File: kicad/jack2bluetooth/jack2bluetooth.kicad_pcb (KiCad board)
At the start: 4 copper layers, 83 x 53 mm, 108 parts, among them IC1 TLV320AIC3101IRHBR, IC2 BQ25619RTWR, IC3 ESP32-C6-WROOM-1-N8, IC4 TPS62A01PDDCR, IC5 TPS62A01PDDCR, IC6 DS04-254-2-02BK-SMT, J1 SJ1-2503A, J2 USB_C_Receptacle, J3 Conn_01x04_Pin, J4 SJ3-35063A, J5 Conn_01x03_Pin, J6 Conn_01x04_Pin, J7 Conn_01x02_Pin, J9 Conn_01x08_Pin, Q1 DMP3099L-13, SW1 SW_Push, SW2 SW_Push, SW3 SW_Push, SW5 SW_SPDT, SW6 SW_Push, U1 TLV75801PDBVR

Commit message: feat: remove warnings in ERC errors and warnings in schematic. refresh layout
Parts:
- removed D6: PRTR5V0U2X, Package_TO_SOT_SMD:SOT-143
- removed IC6: DS04-254-2-02BK-SMT, DIP-switch-2:DS04254202BKSMT
- removed JP2: jumper_RCOM, Connector_PinHeader_2.54mm:PinHeader_1x02_P2.54mm_Vertical
- removed JP3: jumper_ROUT, Connector_PinHeader_2.54mm:PinHeader_1x02_P2.54mm_Vertical
- removed JP4: jumper_LCOM, Connector_PinHeader_2.54mm:PinHeader_1x02_P2.54mm_Vertical
- removed JP5: jumper_LOUT, Connector_PinHeader_2.54mm:PinHeader_1x02_P2.54mm_Vertical
- removed R30, R31: 0, Resistor_SMD:R_0805_2012Metric_Pad1.20x1.40mm_HandSolder
- removed U1: TLV75801PDBVR, TLV75801PDBVR:SOT95P280X145-5N
- added C34: 1u, Capacitor_SMD:C_0805_2012Metric_Pad1.18x1.45mm_HandSolder, F.Cu at (-78.2, 10.3)
- added C35: 0.1uF, Capacitor_SMD:C_0805_2012Metric_Pad1.18x1.45mm_HandSolder, F.Cu at (-78.2, 13.3)
- added C38: 0.1uF, Capacitor_SMD:C_0805_2012Metric_Pad1.18x1.45mm_HandSolder, F.Cu at (-78.2, 16.3)
- added C39: 1uF, Capacitor_SMD:C_0805_2012Metric_Pad1.18x1.45mm_HandSolder, F.Cu at (-78.2, 19.3)
- added C40: 1uF, Capacitor_SMD:C_0805_2012Metric_Pad1.18x1.45mm_HandSolder, F.Cu at (-78.2, 22.4)
- added C41: 1uF, Capacitor_SMD:C_0805_2012Metric_Pad1.18x1.45mm_HandSolder, F.Cu at (-78.2, 25.4)
- added C42: 1uF, Capacitor_SMD:C_0805_2012Metric_Pad1.18x1.45mm_HandSolder, F.Cu at (-78.2, 28.4)
- added C43: 100uF, Capacitor_SMD:C_0805_2012Metric_Pad1.18x1.45mm_HandSolder, F.Cu at (129.9, 298.7)
- added D2: LED - green, LED_SMD:LED_0805_2012Metric_Pad1.15x1.40mm_HandSolder, F.Cu at (-53.2, 41.3)
- added D3: 1N5819, Diode_SMD:D_SOD-123, F.Cu at (171.0, 97.5)
- added F1: Polyfuse, Fuse:Fuse_1210_3225Metric_Pad1.42x2.65mm_HandSolder, F.Cu at (165.0, 97.5)
- added F2: Polyfuse, Fuse:Fuse_1210_3225Metric_Pad1.42x2.65mm_HandSolder, F.Cu at (141.4, 302.2)
- added IC7: ESP32-WROVER-E-N16R8, ESP32-WROVER-E-N16R8:ESP32WROVEREN16R8, F.Cu at (29.9, 51.2)
- added J10: Conn_01x03_Pin, Connector_PinHeader_2.54mm:PinHeader_1x03_P2.54mm_Vertical, F.Cu at (-59.5, 56.5)
- added J8: Conn_01x02_Pin, Connector_PinHeader_2.00mm:PinHeader_1x02_P2.00mm_Vertical, F.Cu at (-66.0, 82.0)
- added PS1: TLV75801PDBVR, TLV75801PDBVR:SOT95P280X145-5N, F.Cu at (341.2, 34.0)
- added Q2: BC846, Package_TO_SOT_SMD:SOT-23, F.Cu at (-128.2, 8.50)
- added Q3: BC846, Package_TO_SOT_SMD:SOT-23, F.Cu at (-136.2, 10.5)
- added SW4: SW_Push, Button_Switch_THT:SW_PUSH_6mm, F.Cu at (-100.7, 45.3)
- added SW7: SW_SPDT, SLW-10558:SLW-105558-2A-N-D, F.Cu at (30.0, 114.5)
- added TP1: TestPoint, TestPoint:TestPoint_Pad_D1.0mm, F.Cu at (123.5, -41.1)
- added TP10: TestPoint, TestPoint:TestPoint_Pad_D1.0mm, F.Cu at (191.4, 297.3)
- added TP11: TestPoint, TestPoint:TestPoint_Pad_D1.0mm, F.Cu at (191.4, 300.3)
- added TP12: TestPoint, TestPoint:TestPoint_Pad_D1.0mm, F.Cu at (191.4, 303.4)
- added TP13: TestPoint, TestPoint:TestPoint_Pad_D1.0mm, F.Cu at (191.4, 306.4)
- added TP14: TestPoint, TestPoint:TestPoint_Pad_D1.0mm, F.Cu at (191.4, 309.5)
- added TP15: TestPoint, TestPoint:TestPoint_Pad_D1.0mm, F.Cu at (194.5, 291.2)
- added TP16: TestPoint, TestPoint:TestPoint_Pad_D1.0mm, F.Cu at (194.5, 294.2)
- added TP17: TestPoint, TestPoint:TestPoint_Pad_D1.0mm, F.Cu at (194.5, 297.3)
- added TP18: TestPoint, TestPoint:TestPoint_Pad_D1.0mm, F.Cu at (194.5, 300.3)
- added TP19: TestPoint, TestPoint:TestPoint_Pad_D1.0mm, F.Cu at (194.5, 303.4)
- added TP2: TestPoint, TestPoint:TestPoint_Pad_D1.0mm, F.Cu at (123.5, -38.1)
- added TP20: TestPoint, TestPoint:TestPoint_Pad_D1.0mm, F.Cu at (194.5, 306.4)
- added TP21: TestPoint, TestPoint:TestPoint_Pad_D1.0mm, F.Cu at (194.5, 309.5)
- added TP22: TestPoint, TestPoint:TestPoint_Pad_D1.0mm, F.Cu at (185.9, 312.2)
- added TP23: TestPoint, TestPoint:TestPoint_Pad_D1.0mm, F.Cu at (213.9, 33.9)
- added TP24: TestPoint, TestPoint:TestPoint_Pad_D1.0mm, F.Cu at (213.9, 37.0)
- added TP25: TestPoint, TestPoint:TestPoint_Pad_D1.0mm, F.Cu at (213.9, 40.0)
- added TP26: TestPoint, TestPoint:TestPoint_Pad_D1.0mm, F.Cu at (213.9, 43.0)
- added TP27: TestPoint, TestPoint:TestPoint_Pad_D1.0mm, F.Cu at (213.9, 46.1)
- added TP28: TestPoint, TestPoint:TestPoint_Pad_D1.0mm, F.Cu at (213.9, 49.1)
- added TP29: TestPoint, TestPoint:TestPoint_Pad_D1.0mm, F.Cu at (217.0, 30.9)
- added TP3: TestPoint, TestPoint:TestPoint_Pad_D1.0mm, F.Cu at (123.5, -35.0)
- added TP30: TestPoint, TestPoint:TestPoint_Pad_D1.0mm, F.Cu at (217.0, 33.9)
- added TP31: TestPoint, TestPoint:TestPoint_Pad_D1.0mm, F.Cu at (217.0, 37.0)
- added TP32: TestPoint, TestPoint:TestPoint_Pad_D1.0mm, F.Cu at (217.0, 40.0)
- added TP33: TestPoint, TestPoint:TestPoint_Pad_D1.0mm, F.Cu at (217.0, 43.0)
- added TP34: TestPoint, TestPoint:TestPoint_Pad_D1.0mm, F.Cu at (217.0, 46.1)
- added TP4: TestPoint, TestPoint:TestPoint_Pad_D1.0mm, F.Cu at (123.5, -32.0)
- added TP5: TestPoint, TestPoint:TestPoint_Pad_D1.0mm, F.Cu at (123.5, -28.9)
- added TP6: TestPoint, TestPoint:TestPoint_Pad_D1.0mm, F.Cu at (123.5, -25.9)
- added TP7: TestPoint, TestPoint:TestPoint_Pad_D1.0mm, F.Cu at (123.5, -22.9)
- added TP8: TestPoint, TestPoint:TestPoint_Pad_D1.0mm, F.Cu at (191.4, 291.2)
- added TP9: TestPoint, TestPoint:TestPoint_Pad_D1.0mm, F.Cu at (191.4, 294.2)
- D1, D4, D7, D8, J7, J9, R7, R8: moved to F.Cu
- D5: value PRTR5V0U2X -> SMF5V0A-E3-08; footprint Package_TO_SOT_SMD:SOT-143 -> LIB_SMF5V0A-E3-08:SMF5V0AE308
- IC1: footprint TLV320AIC3101:QFN50P500X500X100-33N-D -> TLV320AIC3101IRHBR:QFN50P500X500X100-33N-D
- IC3: value ESP32-C6-WROOM-1-N8 -> MCP23008T-E_SO; footprint ESP32-C6-WROOM-1:ESP32C6WROOM1N8 -> LIB_MCP23008T-E_SO:SOIC127P1030X265-18N
- IC4, IC5: footprint TPS62A01PDDRC:SOT95P280X110-6N -> TPS62A01PDDCR:SOT95P280X110-6N
- J1: value SJ1-2503A -> SJ3-35063A; footprint SJ1-2503A:SJ12503A -> LIB_SJ3-35063A:SJ335063A
- J3: value Conn_01x04_Pin -> Conn_01x03_Pin; footprint Connector_PinHeader_2.54mm:PinHeader_1x04_P2.54mm_Vertical -> Connector_PinHeader_2.54mm:PinHeader_1x03_P2.54mm_Vertical
- J4: value SJ3-35063A -> SJ1-2503A; footprint SJ3-35063A:SJ335063A -> LIB_SJ1-2503A:SJ12503A
- Q1: footprint DMP3099L:SOT96P240X115-3N -> DMP3099L-13:SOT96P240X115-3N
- R10: value 0 -> 10k
- R12, R18: value 10k -> 0
- R9: value 0 -> 1k
- moved SW6 316.5 mm to (-117.5, 46.8)
- moved R12 309.9 mm to (-58.2, 16.2)
- moved R10 306.6 mm to (-58.2, 13.2), turned to 0 degrees
- moved R9 305.9 mm to (-58.2, 10.3), turned to 0 degrees
- moved R17 296.9 mm to (-58.2, 22.1), turned to 0 degrees
- moved R16 296.6 mm to (-58.2, 19.1), turned to 0 degrees
- moved J3 283.1 mm to (-89.9, 45.6), turned to 0 degrees
- moved R18 244.2 mm to (-58.2, 25.0), turned to 0 degrees
- moved Q1 237.4 mm to (-58.1, 42.1)
- moved D4 174.0 mm to (123.0, 252.7), turned to 0 degrees
- moved R7 168.0 mm to (115.2, 254.0)
- moved R8 167.4 mm to (109.2, 254.0)
- moved C28 163.3 mm to (340.0, 41.5)
- moved C31 163.3 mm to (346.2, 38.7)
- moved C32 163.3 mm to (333.2, 45.2)
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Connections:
- net /BTST renamed TP_BTST
- net /SW renamed TP_SW
- net Net-(IC2-PMID) renamed TP_PMID
- net Net-(IC2-PMID_GOOD) renamed PMID_GOOD
- C1 pad 2: IO4 -> IO_EXP_1
- C10 pad 2: BAT- -> lcd_cs
- C11 pad 2: BAT- -> lcd_cs
- C16 pad 1: BAT- -> lcd_cs
- C17 pad 2: BAT- -> lcd_cs
- C2 pad 2: IO0 -> IO_EXP_0
- C20 pad 1: Net-(JP2-B) -> HPROUT
- C20 pad 2: jack35_right -> Net-(C20-Pad2)
- C21 pad 1: Net-(JP4-B) -> HPLOUT
- C21 pad 2: jack35_left -> Net-(C21-Pad2)
- C22 pad 1: BAT- -> lcd_cs
- C24 pad 2: BAT- -> lcd_cs
- C25 pad 1: IO1 -> IO_EXP_3
- C25 pad 2: BAT- -> lcd_cs
- C26 pad 1: BAT- -> lcd_cs
- C27 pad 2: BAT- -> lcd_cs
- C28 pad 2: BAT- -> lcd_cs
- C29 pad 2: BAT- -> lcd_cs
- C3 pad 2: IO5 -> IO_EXP_2
- C30 pad 2: BAT- -> lcd_cs
- C32 pad 2: BAT- -> lcd_cs
- C33 pad 2: BAT- -> lcd_cs
- C36 pad 2: BAT- -> lcd_cs
- C37 pad 2: BAT- -> lcd_cs
- C4 pad 2: BAT- -> lcd_cs
- C5 pad 2: BAT- -> lcd_cs
- C6 pad 2: BAT- -> lcd_cs
- C7 pad 2: BAT- -> lcd_cs
- C8 pad 2: LINE2R -> Net-(C8-Pad2)
- C9 pad 2: LINE2L -> Net-(C9-Pad2)
- D1 pad 1: BAT- -> lcd_cs
- D4 pad 2: led_adc -> IO_EXP_4
- D5 pad 1: BAT- -> lcd_cs
- D5 pad 2: USB_DN -> /usb_vbus
- D7 pad 2: led_dac -> IO_EXP_5
- IC1 pad 1: IO19 -> TXD0
- IC1 pad 2: IO20 -> IO2
- IC1 pad 20: HPLCOM -> unconnected-(IC1-HPLCOM-Pad20)
- IC1 pad 22: HPRCOM -> unconnected-(IC1-HPRCOM-Pad22)
- IC1 pad 3: IO21 -> IO4
- IC1 pad 31: IO18 -> IO_EXP_7
- IC1 pad 4: IO22 -> IO5
- IC1 pad 5: IO23 -> IO18
- IC1 pad 6: BAT- -> lcd_cs
- IC1 pad 8: IO7 -> IO21
- IC1 pad 9: IO6 -> IO19
- IC2 pad 15: SYSTEM -> PMIC_SYSTEM
- IC2 pad 16: SYSTEM -> PMIC_SYSTEM
- IC2 pad 17: BAT- -> lcd_cs
- IC2 pad 18: BAT- -> lcd_cs
- IC2 pad 25: BAT- -> lcd_cs
- IC2 pad 5: IO7 -> IO21
- IC2 pad 6: IO6 -> IO19
- IC2 pad 7: IO10 -> IO39
- IC2 pad 9: IO11 -> IO27
- IC3 pad 1: BAT- -> IO21
- IC3 pad 10: IO8 -> IO_EXP_0
- IC3 pad 11: IO10 -> IO_EXP_1
- IC3 pad 12: IO11 -> IO_EXP_2
- IC3 pad 13: USB_DN -> IO_EXP_3
- IC3 pad 14: USB_DP -> IO_EXP_4
- IC3 pad 15: IO9 -> IO_EXP_5
- IC3 pad 16: IO18 -> IO_EXP_6
- IC3 pad 17: IO19 -> IO_EXP_7
- IC3 pad 18: IO20 -> Net-(IC3-VDD)
- IC3 pad 2: +3.3V -> IO19
- IC3 pad 3: mcu_enable -> lcd_cs
- IC3 pad 4: IO4 -> lcd_cs
- IC3 pad 5: IO5 -> lcd_cs
- IC3 pad 6: IO6 -> IO32
- IC3 pad 7: IO7 -> unconnected-(IC3-NC-Pad7)
- IC3 pad 8: IO0 -> IO36
- IC3 pad 9: IO1 -> lcd_cs
- IC4 pad 2: BAT- -> lcd_cs
- IC5 pad 2: BAT- -> lcd_cs
- J1 pad 2: jack25_left -> jack35_right
- J1 pad 3: jack25_left -> jack35_left
- J2 pad A1: BAT- -> lcd_cs
- J2 pad A12: BAT- -> lcd_cs
- J2 pad A4: VCC -> /usb_vbus
- J2 pad A6: USB_DP -> unconnected-(J2-D+-PadA6)
- J2 pad A7: USB_DN -> unconnected-(J2-D--PadA7)
- J2 pad A9: VCC -> /usb_vbus
- J2 pad B1: BAT- -> lcd_cs
- J2 pad B12: BAT- -> lcd_cs
- J2 pad B4: VCC -> /usb_vbus
- J2 pad B6: USB_DP -> unconnected-(J2-D+-PadB6)
- J2 pad B7: USB_DN -> unconnected-(J2-D--PadB7)
- J2 pad B9: VCC -> /usb_vbus
- J2 pad S1: BAT- -> lcd_cs
- J3 pad 1: VCC -> TXD0
- J3 pad 2: IO16 -> RXD0
- J3 pad 3: IO17 -> lcd_cs
- J4 pad 2: jack35_right -> jack25_left
- J4 pad 3: jack35_left -> jack25_left
- J5 pad 2: BAT- -> lcd_cs
- J5 pad 3: BAT+ -> Net-(J5-Pin_3)
- J6 pad 1: IO4 -> IO14
- J6 pad 2: IO5 -> IO12
- J6 pad 3: IO6 -> IO13
- J6 pad 4: IO7 -> IO15
- J7 pad 1: BAT- -> lcd_cs
- J9 pad 2: BAT- -> lcd_cs
- J9 pad 3: IO17 -> IO26
- J9 pad 4: IO15 -> IO25
- J9 pad 5: IO16 -> IO23
- J9 pad 6: IO3 -> IO22
- J9 pad 7: BAT- -> lcd_cs
- JP1 pad 3: BAT- -> lcd_cs
- Q1 pad 1: IO2 -> IO_EXP_6
- R1 pad 1: BAT- -> lcd_cs
- R1 pad 2: IO4 -> IO_EXP_1
- R10 pad 1: LINE2L -> REGN
- R10 pad 2: jack25_left -> Net-(JP1-A)
- R12 pad 1: REGN -> LINE2R
- R12 pad 2: Net-(JP1-A) -> Net-(C8-Pad2)
- R14 pad 2: BAT- -> lcd_cs
- R16 pad 1: jack35_right -> LINE2L
- R16 pad 2: Net-(JP2-B) -> Net-(C9-Pad2)
- R17 pad 1: jack35_left -> jack35_right
- R17 pad 2: Net-(JP4-B) -> Net-(C20-Pad2)
- R18 pad 1: IO9 -> jack35_left
- R18 pad 2: +3.3V -> Net-(C21-Pad2)
- R19 pad 1: IO7 -> IO21
- R2 pad 1: BAT- -> lcd_cs
- R2 pad 2: IO0 -> IO_EXP_0
- R20 pad 1: IO6 -> IO19
- R21 pad 1: IO8 -> lcd_cs
- R21 pad 2: +3.3V -> Net-(Q2-B)
- R23 pad 2: BAT- -> lcd_cs
- R29 pad 1: IO11 -> IO27
- R3 pad 1: BAT- -> lcd_cs
- R3 pad 2: IO5 -> IO_EXP_2
- R32 pad 1: IO10 -> IO39
- R34 pad 1: IO2 -> IO_EXP_6
- R37 pad 2: BAT- -> lcd_cs
- R40 pad 2: BAT- -> lcd_cs
- R5 pad 2: BAT- -> lcd_cs
- R6 pad 1: BAT- -> lcd_cs
- R7 pad 2: BAT- -> lcd_cs
- R8 pad 2: BAT- -> lcd_cs
- R9 pad 1: LINE2R -> SYSTEM
- R9 pad 2: jack25_right -> Net-(D2-A)
- SW1 pad 1: IO4 -> IO_EXP_1
- SW2 pad 1: IO0 -> IO_EXP_0
- SW3 pad 1: IO5 -> IO_EXP_2
- SW5 pad 2: IO1 -> IO_EXP_3
- SW5 pad 3: BAT- -> lcd_cs
- SW6 pad 1: BAT- -> lcd_cs
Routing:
- net BAT-: track 167.8 -> 0.00 mm, vias 38 -> 0
- net nQON: track 108.2 -> 0.00 mm, vias 1 -> 0
- net IO7: track 104.7 -> 0.00 mm, vias 3 -> 0
- net IO9: track 102.0 -> 0.00 mm, vias 5 -> 0
- net IO6: track 101.2 -> 0.00 mm, vias 3 -> 0
- net IO8: track 93.5 -> 0.00 mm, vias 3 -> 0
- net IO5: track 90.7 -> 0.00 mm, vias 2 -> 0
- net Net-(D1-A): track 86.9 -> 0.00 mm, vias 1 -> 0
- net STAT: track 78.7 -> 0.00 mm, vias 1 -> 0
- net IO17: track 72.9 -> 0.00 mm, vias 2 -> 0
- net IO16: track 70.1 -> 0.00 mm, vias 2 -> 0
- net USB_DP: track 68.0 -> 0.00 mm
- net IO1: track 67.8 -> 0.00 mm, vias 1 -> 0
- net USB_DN: track 67.3 -> 0.00 mm
- net IO10: track 62.3 -> 0.00 mm, vias 2 -> 0
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- removed copper zone on In2.Cu, net +1V8
- removed copper zone on In2.Cu, net +3.3V
- removed copper zone on In2.Cu, net +3.3VA
- removed copper zone on B.Cu, net BAT-
- removed copper zone on F.Cu, net BAT-
- removed copper zone on In1.Cu, net BAT-
- removed copper zone on B.Cu, net GNDA
- removed copper zone on F.Cu, net GNDA
- removed copper zone on In1.Cu, net GNDA
- removed copper zone on In2.Cu, net REGN
- removed copper zone on In2.Cu, net SYSTEM
- removed copper zone on In2.Cu, net VCC
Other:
- board size 83 x 53 mm -> 167 x 100 mm
- board text added: "Jack <> Bluetooth Converter Paul Capgras Rev 3.1"
- board text removed: "BLK"
- board text removed: "CS"
- board text removed: "DC"
- board text removed: "GND nQON"
- board text removed: "Jack <> Bluetooth Converter Paul Capgras Rev 3.0"
- board text removed: "LCOM"
- board text removed: "LOUT"
- board text removed: "RCOM"
- board text removed: "REGN SEL GND"
- board text removed: "RES"
- board text removed: "ROUT"
- board text removed: "RX"
- board text removed: "SCL"
- board text removed: "SDA"
- board text removed: "TX"
- board text removed: "VCC"
- board text removed: "VDC"

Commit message: feat: finish layout placement
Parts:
- C8, D1, D2, D4, D7, D8, SW7: moved to B.Cu
- J5: moved to F.Cu
- moved Q3 293.6 mm to (146.8, 89.0)
- moved Q2 293.3 mm to (153.7, 89.3)
- moved TP14 281.2 mm to (149.0, 31.5)
- moved TP13 279.4 mm to (152.2, 29.8)
- moved TP12 274.5 mm to (153.5, 31.5)
- moved SW6 272.6 mm to (152.8, 82.2)
- moved J3 271.5 mm to (176.8, 96.8), turned to -90 degrees
- moved F2 271.0 mm to (124.5, 31.7), turned to -90 degrees
- moved J5 270.2 mm to (124.7, 26.5), turned to 90 degrees
- moved TP11 270.1 mm to (156.5, 32.5)
- moved TP17 268.1 mm to (141.5, 34.5)
- moved TP16 267.4 mm to (144.5, 31.5)
- moved TP22 267.1 mm to (154.0, 47.0)
- moved C43 266.9 mm to (131.0, 31.7), turned to 90 degrees
- moved TP21 266.1 mm to (150.5, 47.0)
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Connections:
- net lcd_blk renamed lcd_vdc
- net lcd_cs renamed GND
- C26 pad 2: SYSTEM -> PMIC_SYSTEM
- L1 pad 2: SYSTEM -> PMIC_SYSTEM
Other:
- board size 167 x 100 mm -> 85.8 x 76 mm
- board text removed: "BAT+"
- board text removed: "GND"
- board text removed: "TS"

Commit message: feat: update placement and update pin assignments for easier routing
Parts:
- moved C38 37.5 mm to (120.2, 93.2)
- moved Q2 12.9 mm to (140.8, 88.8), turned to -90 degrees
- moved R32 12.3 mm to (162.8, 56.8), turned to 0 degrees
- moved R29 12.2 mm to (162.8, 59.2), turned to 0 degrees
- moved Q3 10.5 mm to (136.2, 88.8), turned to -90 degrees
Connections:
- IC1 pad 3: IO4 -> IO5
- IC1 pad 4: IO5 -> IO4
- TP25 pad 1: IO4 -> IO5
- TP26 pad 1: IO5 -> IO4

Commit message: feat: route power
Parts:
- moved C34 47.9 mm to (103.8, 33.2), turned to -90 degrees
- moved TP1 47.8 mm to (167.2, 41.2)
- moved R23 43.9 mm to (106.0, 33.2), turned to 90 degrees
- moved R26 42.3 mm to (126.4, 43.3), turned to -90 degrees
- moved R25 39.6 mm to (129.7, 44.5), turned to 180 degrees
- moved PS1 36.9 mm to (129.5, 41.0), turned to -90 degrees
- moved C31 35.1 mm to (132.9, 43.5), turned to -90 degrees
- moved TP3 34.1 mm to (130.5, 47.5), turned to -90 degrees
- moved C28 33.5 mm to (130.2, 37.2), turned to 180 degrees
- moved C25 5.55 mm to (111.2, 53.0)
- moved R22 5.30 mm to (108.8, 53.0)
- moved TP18 5.15 mm to (138.8, 37.0)
- moved C38 1.46 mm to (121.5, 94.0), turned to -90 degrees
- moved J10 0.54 mm to (119.8, 26.5)
- moved C10 0.51 mm to (128.0, 32.2)
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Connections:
- net Net-(D3-K) renamed /VBUS_con
- net Net-(J5-Pin_3) renamed /BAT+_Connector
- C38 pad 2: Net-(IC3-VDD) -> GND
- IC3 pad 18: Net-(IC3-VDD) -> +3.3V
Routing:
- net VCC: track 0.00 -> 88.0 mm, vias 0 -> 3
- net +3.3V: track 0.00 -> 69.5 mm, vias 0 -> 14
- net +1V8: track 0.00 -> 58.9 mm, vias 0 -> 4
- net REGN: track 0.00 -> 47.9 mm, vias 0 -> 3
- net BAT+: track 0.00 -> 45.7 mm
- net SYSTEM: track 0.00 -> 42.6 mm, vias 0 -> 6
- net PMIC_SYSTEM: track 0.00 -> 38.5 mm, vias 0 -> 1
- net +3.3VA: track 0.00 -> 30.4 mm, vias 0 -> 6
- net GND: track 0.00 -> 15.9 mm, vias 0 -> 46
- net TP_PMID: track 0.00 -> 11.1 mm
- net TP_SW: track 0.00 -> 10.6 mm
- net /usb_vbus: track 0.00 -> 10.2 mm
- net BATTS: track 0.00 -> 9.54 mm
- net HPROUT: track 0.00 -> 9.39 mm
- net HPLOUT: track 0.00 -> 9.29 mm
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- added copper zone on In2.Cu, net +3.3V
- added copper zone on In2.Cu, net +3.3VA
- added copper zone on In1.Cu, net GND
- added copper zone on In1.Cu, net GNDA
- added copper zone on In2.Cu, net SYSTEM

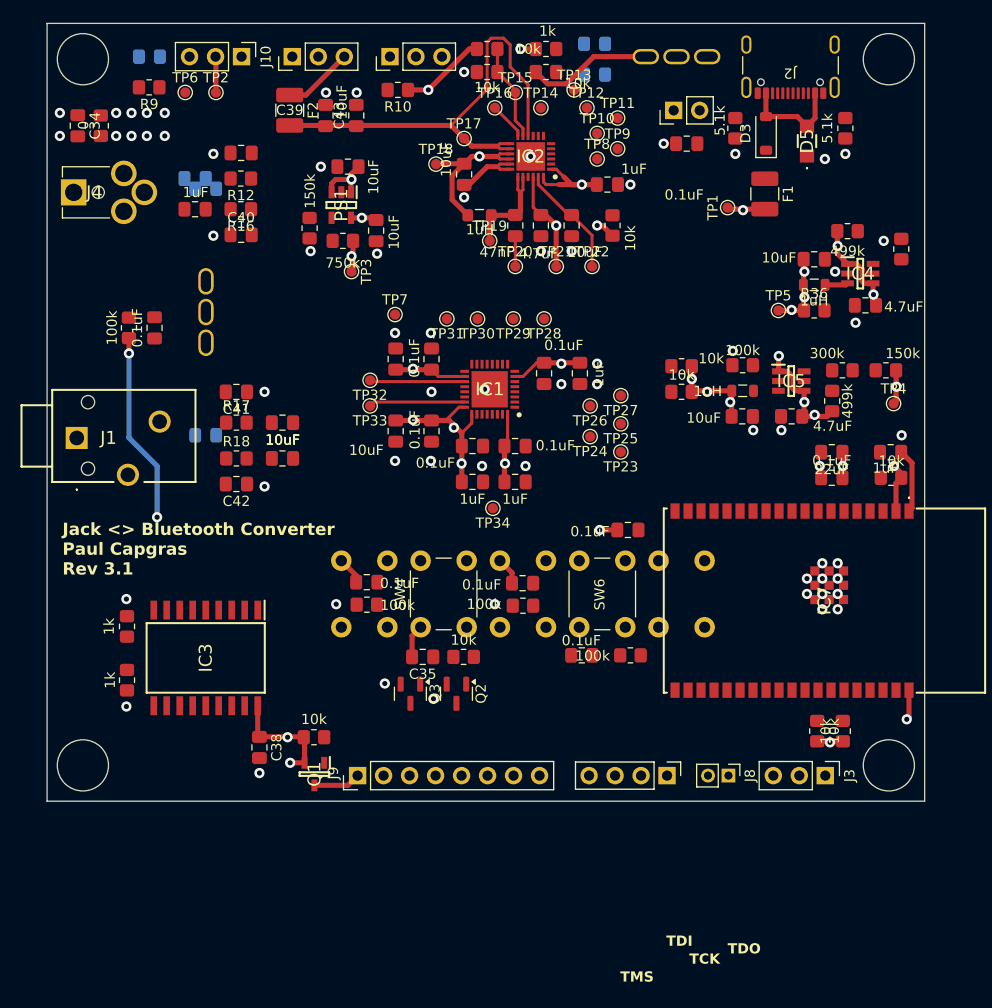
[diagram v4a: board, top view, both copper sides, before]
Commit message: feat: routing done, silkscreen done
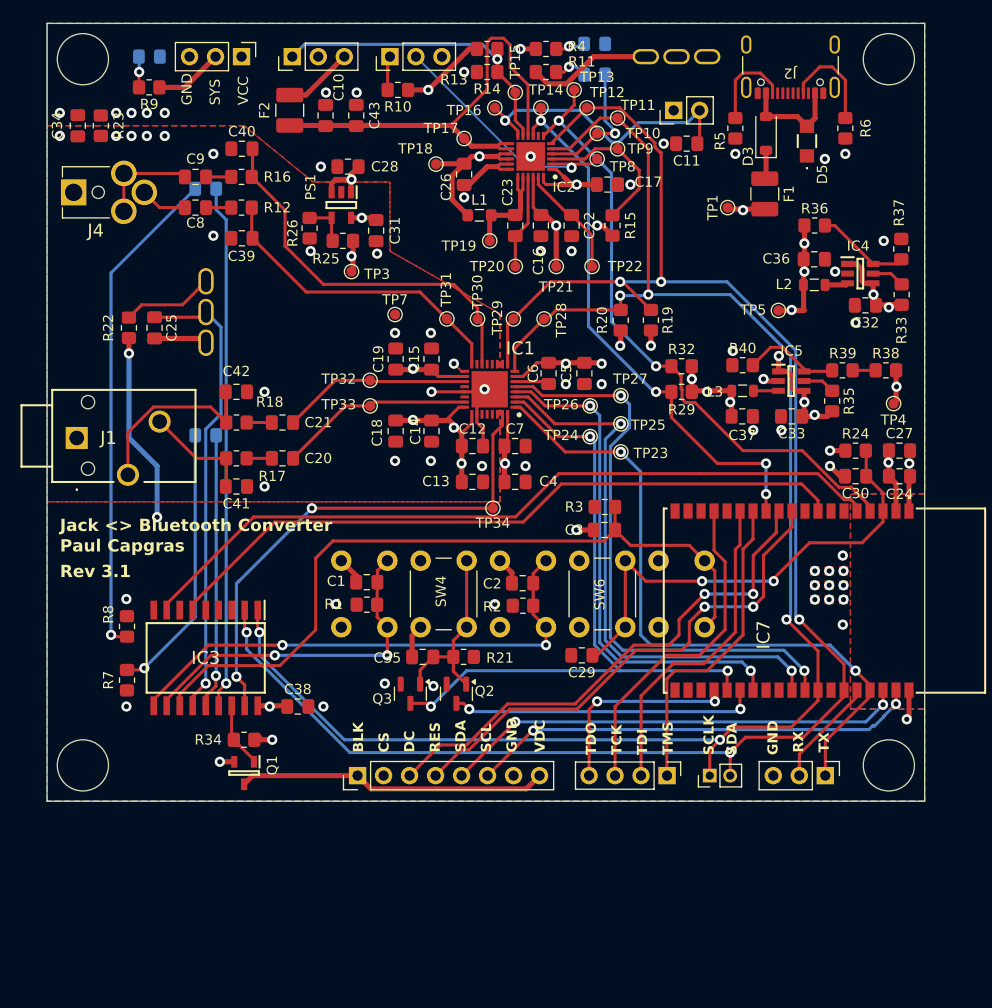
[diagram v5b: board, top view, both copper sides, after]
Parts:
- removed TP2, TP6: TestPoint, TestPoint:TestPoint_Pad_D1.0mm
- C8: moved to F.Cu
- moved R20 44.5 mm to (156.8, 52.2)
- moved R19 44.3 mm to (159.8, 52.2)
- moved R3 14.7 mm to (155.2, 70.5)
- moved C41 9.24 mm to (119.2, 68.5)
- moved C42 9.01 mm to (119.2, 59.2)
- moved C40 8.41 mm to (119.8, 35.5)
- moved C39 8.34 mm to (119.8, 44.2)
- moved R36 8.30 mm to (175.8, 43.0)
- moved R33 8.15 mm to (184.2, 49.8), turned to -90 degrees
- moved C27 7.12 mm to (184.0, 65.0), turned to 0 degrees
- moved C24 7.02 mm to (184.0, 67.5), turned to 0 degrees
- moved Q1 6.87 mm to (120.0, 96.5)
- moved R34 6.83 mm to (120.0, 93.2), turned to 0 degrees
- moved C38 5.48 mm to (125.2, 90.0), turned to 0 degrees
- moved R24 4.36 mm to (179.8, 65.0), turned to 0 degrees
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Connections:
- net Net-(JP1-A) renamed /POS1
- IC1 pad 8: IO21 -> IO19
- IC1 pad 9: IO19 -> IO21
- IC2 pad 5: IO21 -> IO19
- IC2 pad 6: IO19 -> IO21
- IC2 pad 7: IO39 -> IO36
- IC3 pad 1: IO21 -> IO19
- IC3 pad 2: IO19 -> IO21
- IC3 pad 8: IO36 -> IO39
- J8 pad 1: IO21 -> IO19
- J8 pad 2: IO19 -> IO21
- J9 pad 5: IO23 -> IO22
- J9 pad 6: IO22 -> IO23
- R32 pad 1: IO39 -> IO36
- TP11 pad 1: IO21 -> IO19
- TP12 pad 1: IO19 -> IO21
- TP13 pad 1: IO39 -> IO36
- TP28 pad 1: IO21 -> IO19
- TP29 pad 1: IO19 -> IO21
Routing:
- net IO21: track 0.00 -> 174.9 mm, vias 0 -> 5
- net IO19: track 0.00 -> 164.2 mm, vias 0 -> 5
- net IO39: track 0.00 -> 75.1 mm
- net IO_EXP_2: track 0.00 -> 74.0 mm
- net IO32: track 0.00 -> 68.3 mm
- net IO2: track 0.00 -> 67.4 mm, vias 0 -> 3
- net TXD0: track 0.00 -> 66.1 mm, vias 0 -> 2
- net IO36: track 0.00 -> 62.0 mm, vias 0 -> 2
- net IO18: track 0.00 -> 57.8 mm, vias 0 -> 2
- net IO27: track 0.00 -> 54.9 mm, vias 0 -> 4
- net IO5: track 0.00 -> 54.7 mm, vias 0 -> 2
- net IO_EXP_5: track 0.00 -> 51.0 mm, vias 0 -> 1
- net IO26: track 0.00 -> 51.0 mm, vias 0 -> 2
- net IO_EXP_0: track 0.00 -> 50.2 mm, vias 0 -> 2
- net IO25: track 0.00 -> 50.0 mm, vias 0 -> 2
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- added copper zone on B.Cu, net GND
- added copper zone on F.Cu, net GND
- added copper zone on F.Cu, net GNDA
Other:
- board text added: "BAT+"
- board text added: "BATTS"
- board text added: "BLK"
- board text added: "CS"
- board text added: "DC"
- board text added: "GND"
- board text added: "Jack <> Bluetooth Converter"
- board text added: "POS1"
- board text added: "PSEL"
- board text added: "Paul Capgras"
- board text added: "RES"
- board text added: "RX"
- board text added: "Rev 3.1"
- board text added: "SCL"
- board text added: "SCLK"
- board text added: "SDA"
- board text added: "SYS"
- board text added: "TX"
- board text added: "VCC"
- board text added: "VDC"
- board text added: "nQON"
- board text removed: "Jack <> Bluetooth Converter Paul Capgras Rev 3.1"

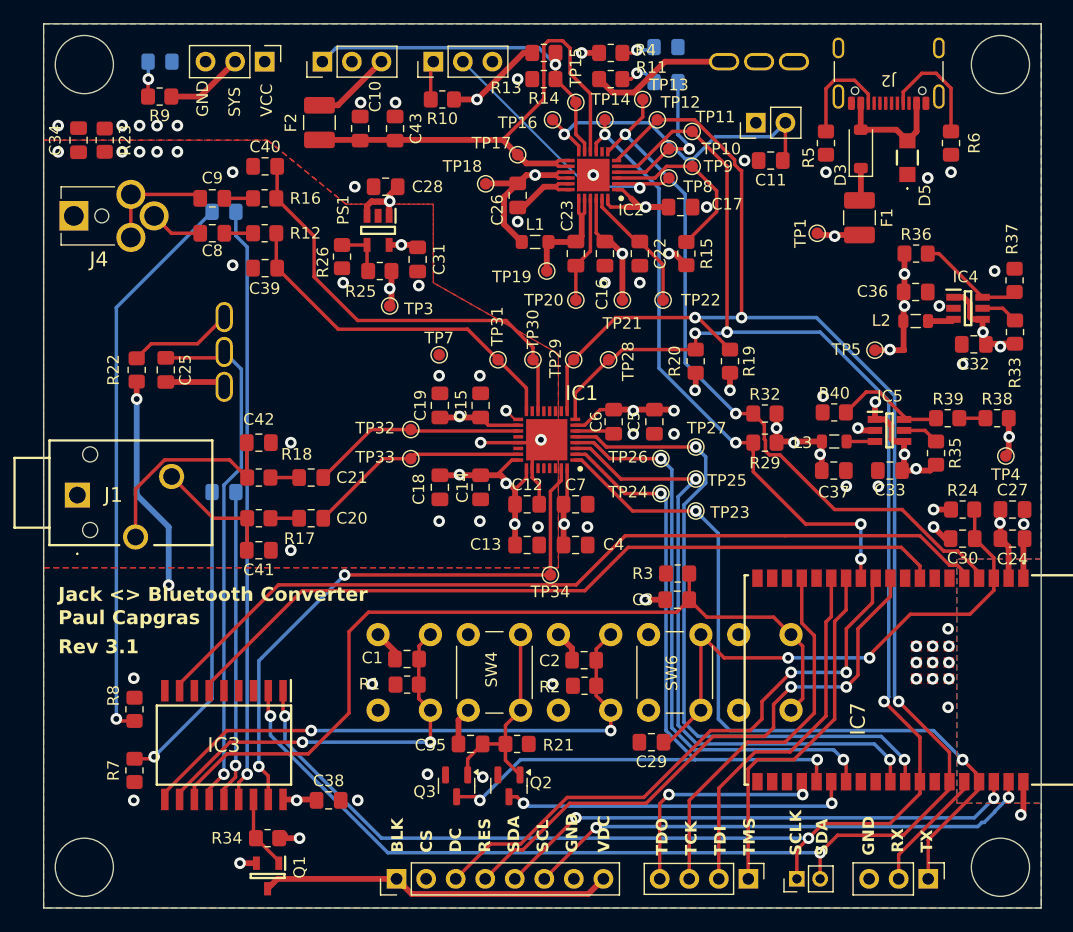
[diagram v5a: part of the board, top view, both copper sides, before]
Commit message: feat: length tuning, custom footprints and update doc
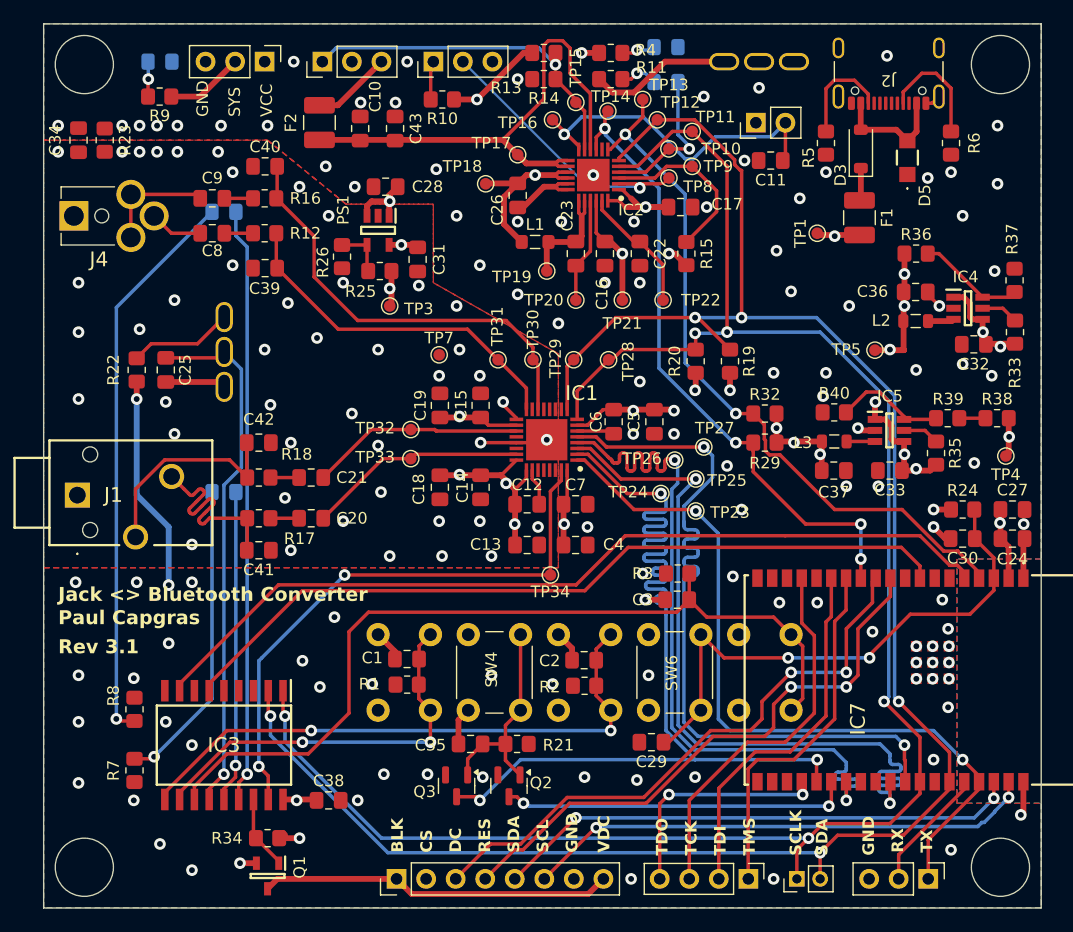
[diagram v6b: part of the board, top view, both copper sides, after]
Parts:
- IC1: footprint TLV320AIC3101IRHBR:QFN50P500X500X100-33N-D -> TLV320AIC3101IRHBR:QFN50P500X500X100-33N-D_custom
- IC2: footprint BQ25619RTWR:QFN50P400X400X80-25N-D -> BQ25619RTWR:QFN50P400X400X80-25N-D_custom
- moved TP26 1.19 mm to (155.0, 60.8)
- moved TP14 0.79 mm to (149.2, 30.8)
- moved TP27 0.69 mm to (157.5, 59.6)
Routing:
- net IO2: track 67.4 -> 86.8 mm
- net IO4: track 49.3 -> 64.8 mm
- net IO5: track 54.7 -> 65.0 mm
- net jack35_right: track 10.8 -> 18.3 mm
- net IO18: track 57.8 -> 64.8 mm
- net GND: track 25.1 -> 27.5 mm, vias 49 -> 109
- net IO27: track 54.9 -> 56.0 mm
- net BAT+: track 45.7 -> 45.1 mm
- net VCC: track 87.6 -> 87.0 mm
- net GNDA: track 13.0 -> 12.7 mm, vias 19 -> 45
